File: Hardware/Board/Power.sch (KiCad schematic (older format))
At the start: 89 parts, among them Q1 Q_NMOS_DGS, Q2 Q_NMOS_DGS, Q3 Q_NMOS_DGS, Q4 Q_NMOS_DGS, U10 MAX17572, U11 MAX17572, U12 MAX17574, U16 STLD40D, U8 MAX17572, U9 MAX17572

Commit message: Trennung MCU und Rest, Footprints fast alles zugewiesen, GSM Modul integriert, viel Kleinkram
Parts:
- D1: footprint (none) -> Diode_SMD:D_SMB
- U16: footprint (none) -> Package_DFN_QFN:DFN-8-1EP_3x3mm_P0.65mm_EP1.55x2.4mm
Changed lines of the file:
@@
 F 0 "U16" H 3650 8125 50  0000 C CNN
 F 1 "STLD40D" H 3650 8034 50  0000 C CNN
-F 2 "" H 3650 8050 50  0001 C CNN
+F 2 "Package_DFN_QFN:DFN-8-1EP_3x3mm_P0.65mm_EP1.55x2.4mm" H 3650 8050 50  0001 C CNN
 F 3 "" H 3650 8050 50  0001 C CNN
 	1    3650 8050
@@
 F 0 "D1" H 4650 8015 50  0000 C CNN
 F 1 "DIODE" H 4650 7924 50  0000 C CNN
-F 2 "" H 4650 7750 50  0001 C CNN
+F 2 "Diode_SMD:D_SMB" H 4650 7750 50  0001 C CNN
 F 3 "~" H 4650 7750 50  0001 C CNN
 	1    4650 7750

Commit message: Footprints zuweisungen
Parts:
- removed Q1, Q2, Q3, Q4: Q_NMOS_DGS, symbol Device:Q_NMOS_DGS
- added Q1, Q2, Q3, Q4: 2N7002, Package_TO_SOT_SMD:SOT-23, symbol Transistor_FET:2N7002
- L1, L2, L3, L6: footprint (none) -> Inductor_SMD:L_Coilcraft_XxL4040
- L4: footprint (none) -> Inductor_SMD:L_Coilcraft_XxL4020
- L5: footprint (none) -> SamacSys_Parts:XAL8080
- L7: footprint (none) -> Inductor_SMD:L_Coilcraft_XxL4030
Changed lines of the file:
@@
 F 0 "L5" V 9840 1850 50  0000 C CNN
 F 1 "10uH" V 9749 1850 50  0000 C CNN
-F 2 "" H 9650 1850 50  0001 C CNN
+F 2 "SamacSys_Parts:XAL8080" H 9650 1850 50  0001 C CNN
 F 3 "~" H 9650 1850 50  0001 C CNN
 	1    9650 1850
@@
 	6700 1750 7050 1750
 $Comp
-L Device:Q_NMOS_DGS Q3
-U 1 1 5CA54BA8
-P 6950 2400
-AR Path="/5C8BBC9A/5CA54BA8" Ref="Q3"  Part="1"
-AR Path="/5E0C5EEA/5CA54BA8" Ref="Q?"  Part="1"
-F 0 "Q3" H 6750 2250 50  0000 L CNN
-F 1 "Q_NMOS_DGS" H 6550 2150 50  0000 L CNN
-F 2 "" H 7150 2500 50  0001 C CNN
-F 3 "~" H 6950 2400 50  0001 C CNN
-	1    6950 2400
-	1    0    0    -1
-$EndComp
-$Comp
 L power:GND #PWR0172
 U 1 1 5CA54C22
@@
 F 0 "L2" V 4840 3650 50  0000 C CNN
 F 1 "15uH" V 4749 3650 50  0000 C CNN
-F 2 "" H 4650 3650 50  0001 C CNN
+F 2 "Inductor_SMD:L_Coilcraft_XxL4040" H 4650 3650 50  0001 C CNN
 F 3 "~" H 4650 3650 50  0001 C CNN
 	1    4650 3650
@@
 F 0 "L1" V 4840 1600 50  0000 C CNN
 F 1 "15uH" V 4749 1600 50  0000 C CNN
-F 2 "" H 4650 1600 50  0001 C CNN
+F 2 "Inductor_SMD:L_Coilcraft_XxL4040" H 4650 1600 50  0001 C CNN
 F 3 "~" H 4650 1600 50  0001 C CNN
 	1    4650 1600
@@
 F 0 "L3" V 4840 5800 50  0000 C CNN
 F 1 "15uH" V 4749 5800 50  0000 C CNN
-F 2 "" H 4650 5800 50  0001 C CNN
+F 2 "Inductor_SMD:L_Coilcraft_XxL4040" H 4650 5800 50  0001 C CNN
 F 3 "~" H 4650 5800 50  0001 C CNN
 	1    4650 5800
@@
 	5100 6550 5100 6600
 $Comp
-L Device:Q_NMOS_DGS Q1
-U 1 1 5CAED088
-P 2200 4250
-AR Path="/5C8BBC9A/5CAED088" Ref="Q1"  Part="1"
-AR Path="/5E0C5EEA/5CAED088" Ref="Q?"  Part="1"
-F 0 "Q1" H 1700 4100 50  0000 L CNN
-F 1 "Q_NMOS_DGS" H 1650 4000 50  0000 L CNN
-F 2 "" H 2400 4350 50  0001 C CNN
-F 3 "~" H 2200 4250 50  0001 C CNN
-	1    2200 4250
-	1    0    0    -1
-$EndComp
-$Comp
 L power:GND #PWR0206
 U 1 1 5CAED08F
@@
 $EndComp
 $Comp
-L Device:Q_NMOS_DGS Q2
-U 1 1 5CB04AE3
-P 2200 6400
-AR Path="/5C8BBC9A/5CB04AE3" Ref="Q2"  Part="1"
-AR Path="/5E0C5EEA/5CB04AE3" Ref="Q?"  Part="1"
-F 0 "Q2" H 1700 6200 50  0000 L CNN
-F 1 "Q_NMOS_DGS" H 1650 6100 50  0000 L CNN
-F 2 "" H 2400 6500 50  0001 C CNN
-F 3 "~" H 2200 6400 50  0001 C CNN
-	1    2200 6400
-	1    0    0    -1
-$EndComp
-$Comp
 L power:GND #PWR0207
 U 1 1 5CB04AEA
@@
 F 0 "L4" V 8222 3450 50  0000 C CNN
 F 1 "L_Core_Ferrite" V 8313 3450 50  0000 C CNN
-F 2 "" H 8400 3450 50  0001 C CNN
+F 2 "Inductor_SMD:L_Coilcraft_XxL4020" H 8400 3450 50  0001 C CNN
 F 3 "~" H 8400 3450 50  0001 C CNN
 	1    8400 3450
@@
 F 0 "L6" V 9890 5000 50  0000 C CNN
 F 1 "15uH" V 9799 5000 50  0000 C CNN
-F 2 "" H 9700 5000 50  0001 C CNN
+F 2 "Inductor_SMD:L_Coilcraft_XxL4040" H 9700 5000 50  0001 C CNN
 F 3 "~" H 9700 5000 50  0001 C CNN
 	1    9700 5000
@@
 F 0 "L7" V 3840 7750 50  0000 C CNN
 F 1 "4uH7" V 3749 7750 50  0000 C CNN
-F 2 "" H 3650 7750 50  0001 C CNN
+F 2 "Inductor_SMD:L_Coilcraft_XxL4030" H 3650 7750 50  0001 C CNN
 F 3 "~" H 3650 7750 50  0001 C CNN
 	1    3650 7750
@@
 	7350 5350 7350 5400
 $Comp
-L Device:Q_NMOS_DGS Q4
-U 1 1 5D1E6DA4
+L Transistor_FET:2N7002 Q1
+U 1 1 5D17A6FC
+P 2200 4250
+F 0 "Q1" H 2405 4296 50  0000 L CNN
+F 1 "2N7002" H 2405 4205 50  0000 L CNN
+F 2 "Package_TO_SOT_SMD:SOT-23" H 2400 4175 50  0001 L CIN
+F 3 "https://www.fairchildsemi.com/datasheets/2N/2N7002.pdf" H 2200 4250 50  0001 L CNN
+	1    2200 4250
+	1    0    0    -1
+$EndComp
+$Comp
+L Transistor_FET:2N7002 Q2
+U 1 1 5D17AC62
+P 2200 6400
+F 0 "Q2" H 2405 6446 50  0000 L CNN
+F 1 "2N7002" H 2405 6355 50  0000 L CNN
+F 2 "Package_TO_SOT_SMD:SOT-23" H 2400 6325 50  0001 L CIN
+F 3 "https://www.fairchildsemi.com/datasheets/2N/2N7002.pdf" H 2200 6400 50  0001 L CNN
+	1    2200 6400
+	1    0    0    -1
+$EndComp
+$Comp
+L Transistor_FET:2N7002 Q4
+U 1 1 5D17AD96
 P 7250 5600
-AR Path="/5C8BBC9A/5D1E6DA4" Ref="Q4"  Part="1"
-AR Path="/5E0C5EEA/5D1E6DA4" Ref="Q?"  Part="1"
-F 0 "Q4" H 7050 5450 50  0000 L CNN
-F 1 "Q_NMOS_DGS" H 6700 5350 50  0000 L CNN
-F 2 "" H 7450 5700 50  0001 C CNN
-F 3 "~" H 7250 5600 50  0001 C CNN
+F 0 "Q4" H 7455 5646 50  0000 L CNN
+F 1 "2N7002" H 7455 5555 50  0000 L CNN
+F 2 "Package_TO_SOT_SMD:SOT-23" H 7450 5525 50  0001 L CIN
+F 3 "https://www.fairchildsemi.com/datasheets/2N/2N7002.pdf" H 7250 5600 50  0001 L CNN
 	1    7250 5600
 	1    0    0    -1
 $EndComp
+$Comp
+L Transistor_FET:2N7002 Q3
+U 1 1 5D17B2D6
+P 6950 2400
+F 0 "Q3" H 7155 2446 50  0000 L CNN
+F 1 "2N7002" H 7155 2355 50  0000 L CNN
+F 2 "Package_TO_SOT_SMD:SOT-23" H 7150 2325 50  0001 L CIN
+F 3 "https://www.fairchildsemi.com/datasheets/2N/2N7002.pdf" H 6950 2400 50  0001 L CNN
+	1    6950 2400
+	1    0    0    -1
+$EndComp

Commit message: Komplete enummerierung Geändert, Schaltplan zusammengefasst, Layout nochmals reset. BOM zu 75% fertig gestellt
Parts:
- added D101, D102: B345BE-13, Diode_SMD:D_SMB, symbol pspice:DIODE
- C100: renamed from C26; footprint Capacitor_SMD:C_0603_1608Metric -> Capacitor_SMD:C_1210_3225Metric
- C105: renamed from C27; footprint Capacitor_SMD:C_0603_1608Metric -> Capacitor_SMD:C_1210_3225Metric
- C111: renamed from C28; footprint Capacitor_SMD:C_0603_1608Metric -> Capacitor_SMD:C_1210_3225Metric
- C117: renamed from C67; footprint Capacitor_SMD:C_0603_1608Metric -> Capacitor_SMD:C_1210_3225Metric
- C119: renamed from C69; footprint Capacitor_SMD:C_0603_1608Metric -> Capacitor_SMD:C_1210_3225Metric
- C120: renamed from C40; footprint Capacitor_SMD:C_0603_1608Metric -> Capacitor_SMD:C_1210_3225Metric
- C121: renamed from C41; footprint Capacitor_SMD:C_0603_1608Metric -> Capacitor_SMD:C_1210_3225Metric
- C132: renamed from C42; footprint Capacitor_SMD:C_0603_1608Metric -> Capacitor_SMD:C_1210_3225Metric
- D100: renamed from D1; value DIODE -> B345BE-13
- renumbered C33 to C101, C37 to C102, C29 to C104, C32 to C106, C34 to C107, C38 to C108, C36 to C109, C30 to C110, C35 to C112, C39 to C113, C31 to C114, C65 to C115, C66 to C116, C68 to C118, C44 to C122, C48 to C123, C56 to C124, C54 to C125, C57 to C126, C51 to C127, C43 to C128, C45 to C129, C49 to C130, C53 to C131, C46 to C133, C47 to C134, C50 to C135, C55 to C136, C52 to C137, FB16 to FB100, FB17 to FB101, L1 to L100, L2 to L101, L3 to L102, L7 to L103, L5 to L104, L4 to L105, L6 to L106, Q1 to Q100, Q2 to Q102, Q3 to Q103, Q4 to Q104, R14 to R100, R15 to R101, R18 to R102, R22 to R103, R23 to R104, R12 to R105, R16 to R106, R19 to R107, R21 to R108, R24 to R109, R25 to R110, R13 to R111, R17 to R112, R20 to R113, R26 to R114, R27 to R115, R50 to R116, R51 to R117, R52 to R118, R28 to R119, R30 to R120, R32 to R121, R35 to R122, R38 to R123, R39 to R124, R29 to R125, R31 to R126, R33 to R127, R36 to R128, R37 to R129, R34 to R130, U8 to U100, U9 to U101, U10 to U102, U16 to U103, U12 to U104, U11 to U105
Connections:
- net DC_Input: now also D101.2 (A), D102.2 (A)
- net GND: now also D101.1 (K), D102.1 (K)
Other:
- moved on the sheet: C128, C129

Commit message: Bauteil Gruppierungen im Layout
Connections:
- net +BATT: now also L105.1; no longer F1.1
- net DC_Input: now also F1.2; no longer D101.2 (A), D102.2 (A), L105.2
- new net: D101.2 (A), D102.2 (A), F1.1, L105.2
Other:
- moved on the sheet: D101, D102, F1, L105
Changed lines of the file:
@@
 L Device:L_Core_Ferrite L105
 U 1 1 5CB6DCC1
-P 8400 3450
+P 8700 3450
 AR Path="/5C8BBC9A/5CB6DCC1" Ref="L105"  Part="1"
 AR Path="/5E0C5EEA/5CB6DCC1" Ref="L?"  Part="1"
-F 0 "L105" V 8200 3550 50  0000 C CNN
-F 1 "L_Core_Ferrite" V 8300 3550 50  0000 C CNN
-F 2 "Inductor_SMD:L_Coilcraft_XxL4020" H 8400 3450 50  0001 C CNN
-F 3 "~" H 8400 3450 50  0001 C CNN
-	1    8400 3450
+F 0 "L105" V 8500 3550 50  0000 C CNN
+F 1 "L_Core_Ferrite" V 8600 3550 50  0000 C CNN
+F 2 "Inductor_SMD:L_Coilcraft_XxL4020" H 8700 3450 50  0001 C CNN
+F 3 "~" H 8700 3450 50  0001 C CNN
+	1    8700 3450
 	0    1    1    0
 $EndComp
@@
 L Device:Fuse F1
 U 1 1 5CB6DEB6
-P 8950 3450
+P 7500 3450
 AR Path="/5C8BBC9A/5CB6DEB6" Ref="F1"  Part="1"
 AR Path="/5E0C5EEA/5CB6DEB6" Ref="F?"  Part="1"
-F 0 "F1" V 8753 3450 50  0000 C CNN
-F 1 "KFZ 5A" V 8844 3450 50  0000 C CNN
-F 2 "Fuse:Fuseholder_Blade_ATO_Littelfuse_Pudenz_2_Pin" V 8880 3450 50  0001 C CNN
-F 3 "~" H 8950 3450 50  0001 C CNN
-	1    8950 3450
+F 0 "F1" V 7303 3450 50  0000 C CNN
+F 1 "KFZ 5A" V 7394 3450 50  0000 C CNN
+F 2 "Fuse:Fuseholder_Blade_ATO_Littelfuse_Pudenz_2_Pin" V 7430 3450 50  0001 C CNN
+F 3 "~" H 7500 3450 50  0001 C CNN
+	1    7500 3450
 	0    1    1    0
 $EndComp
@@
 $EndComp
 Wire Wire Line
-	9100 3450 9400 3450
-Wire Wire Line
 	9650 3450 9400 3450
 Connection ~ 9400 3450
@@
 Connection ~ 9650 3450
 Wire Wire Line
-	8800 3450 8550 3450
-Wire Wire Line
 	6800 3450 7100 3450
-Connection ~ 7100 3450
 Text GLabel 6700 3450 0    50   Input ~ 0
 DC_Input
@@
 L pspice:DIODE D101
 U 1 1 5D54A227
-P 7650 3650
+P 7950 3650
 AR Path="/5C8BBC9A/5D54A227" Ref="D101"  Part="1"
 AR Path="/5E0C5EEA/5D54A227" Ref="D?"  Part="1"
-F 0 "D101" V 8150 4000 50  0000 C CNN
-F 1 "B345BE-13" V 8050 3900 50  0000 C CNN
-F 2 "Diode_SMD:D_SMB" H 7650 3650 50  0001 C CNN
-F 3 "~" H 7650 3650 50  0001 C CNN
-	1    7650 3650
-	0    -1   -1   0
-$EndComp
-$Comp
-L pspice:DIODE D102
-U 1 1 5D584B01
-P 7950 3650
-AR Path="/5C8BBC9A/5D584B01" Ref="D102"  Part="1"
-AR Path="/5E0C5EEA/5D584B01" Ref="D?"  Part="1"
-F 0 "D102" V 8450 3800 50  0000 C CNN
-F 1 "B345BE-13" V 8350 3700 50  0000 C CNN
+F 0 "D101" V 8450 4000 50  0000 C CNN
+F 1 "B345BE-13" V 8350 3900 50  0000 C CNN
 F 2 "Diode_SMD:D_SMB" H 7950 3650 50  0001 C CNN
 F 3 "~" H 7950 3650 50  0001 C CNN
@@
 $EndComp
 $Comp
+L pspice:DIODE D102
+U 1 1 5D584B01
+P 8250 3650
+AR Path="/5C8BBC9A/5D584B01" Ref="D102"  Part="1"
+AR Path="/5E0C5EEA/5D584B01" Ref="D?"  Part="1"
+F 0 "D102" V 8750 3800 50  0000 C CNN
+F 1 "B345BE-13" V 8650 3700 50  0000 C CNN
+F 2 "Diode_SMD:D_SMB" H 8250 3650 50  0001 C CNN
+F 3 "~" H 8250 3650 50  0001 C CNN
+	1    8250 3650
+	0    -1   -1   0
+$EndComp
+$Comp
 L power:GND #PWR0380
 U 1 1 5D5917AD
-P 7650 3850
+P 7950 3850
 AR Path="/5C8BBC9A/5D5917AD" Ref="#PWR0380"  Part="1"
 AR Path="/5E0C5EEA/5D5917AD" Ref="#PWR?"  Part="1"
-F 0 "#PWR0380" H 7650 3600 50  0001 C CNN
-F 1 "GND" H 7655 3677 50  0000 C CNN
-F 2 "" H 7650 3850 50  0001 C CNN
-F 3 "" H 7650 3850 50  0001 C CNN
-	1    7650 3850
-	1    0    0    -1
-$EndComp
-$Comp
-L power:GND #PWR0381
-U 1 1 5D59D0F4
-P 7950 3850
-AR Path="/5C8BBC9A/5D59D0F4" Ref="#PWR0381"  Part="1"
-AR Path="/5E0C5EEA/5D59D0F4" Ref="#PWR?"  Part="1"
-F 0 "#PWR0381" H 7950 3600 50  0001 C CNN
+F 0 "#PWR0380" H 7950 3600 50  0001 C CNN
 F 1 "GND" H 7955 3677 50  0000 C CNN
 F 2 "" H 7950 3850 50  0001 C CNN
@@
 	1    0    0    -1
 $EndComp
+$Comp
+L power:GND #PWR0381
+U 1 1 5D59D0F4
+P 8250 3850
+AR Path="/5C8BBC9A/5D59D0F4" Ref="#PWR0381"  Part="1"
+AR Path="/5E0C5EEA/5D59D0F4" Ref="#PWR?"  Part="1"
+F 0 "#PWR0381" H 8250 3600 50  0001 C CNN
+F 1 "GND" H 8255 3677 50  0000 C CNN
+F 2 "" H 8250 3850 50  0001 C CNN
+F 3 "" H 8250 3850 50  0001 C CNN
+	1    8250 3850
+	1    0    0    -1
+$EndComp
+Wire Wire Line
+	8550 3450 8250 3450
 Wire Wire Line
 	8250 3450 7950 3450
-Wire Wire Line
-	7950 3450 7650 3450
+Connection ~ 8250 3450
+Wire Wire Line
+	8850 3450 9400 3450
+Wire Wire Line
+	7650 3450 7950 3450
 Connection ~ 7950 3450
 Wire Wire Line
-	7100 3450 7650 3450
-Connection ~ 7650 3450
+	7350 3450 7100 3450
+Connection ~ 7100 3450
 $EndSCHEMATC

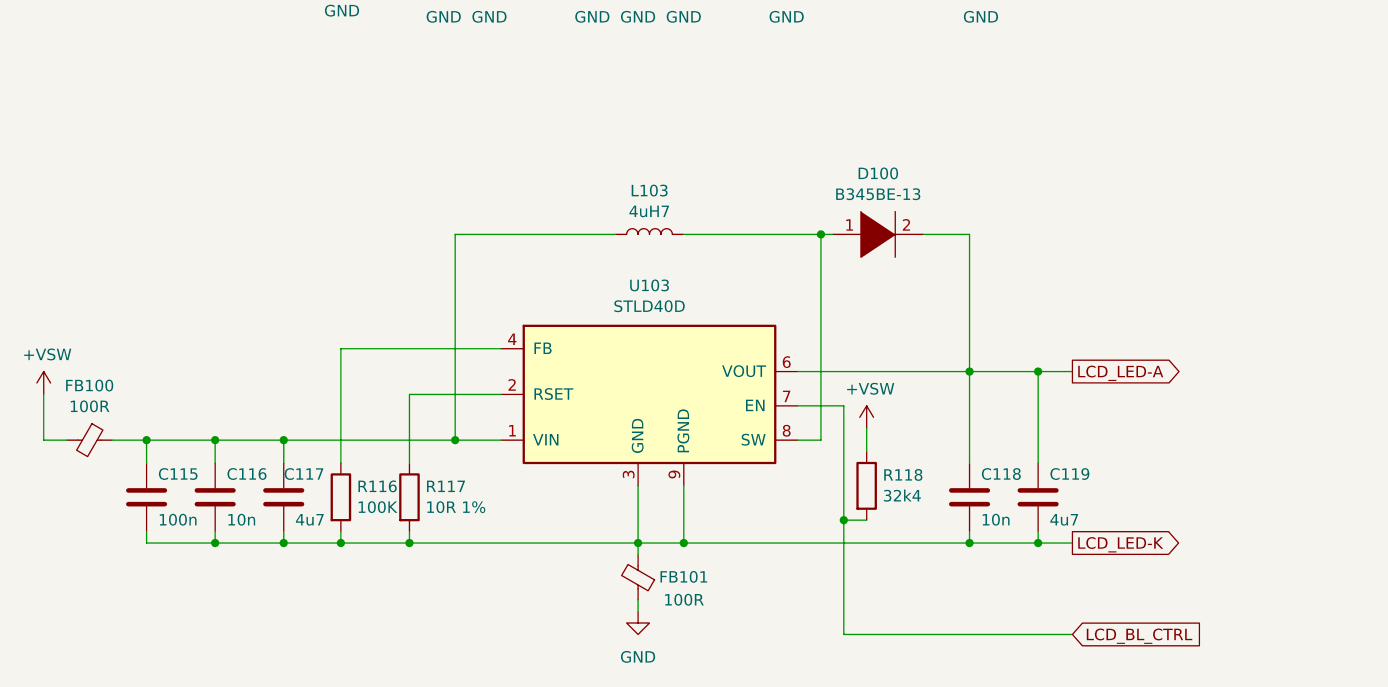
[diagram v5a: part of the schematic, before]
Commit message: Änderung des Konzeptes auf 2 Boards, eines TFT Touch mit STM32L4R9, das rein die Bedienung macht. Control Board mit STM32L476, mit noch mehr Schnittstellen. Bus zwischen Display, Board, Raspberry/ESP ist RS485, Bus als RJ45 mit Wakeup und Stromversorgung
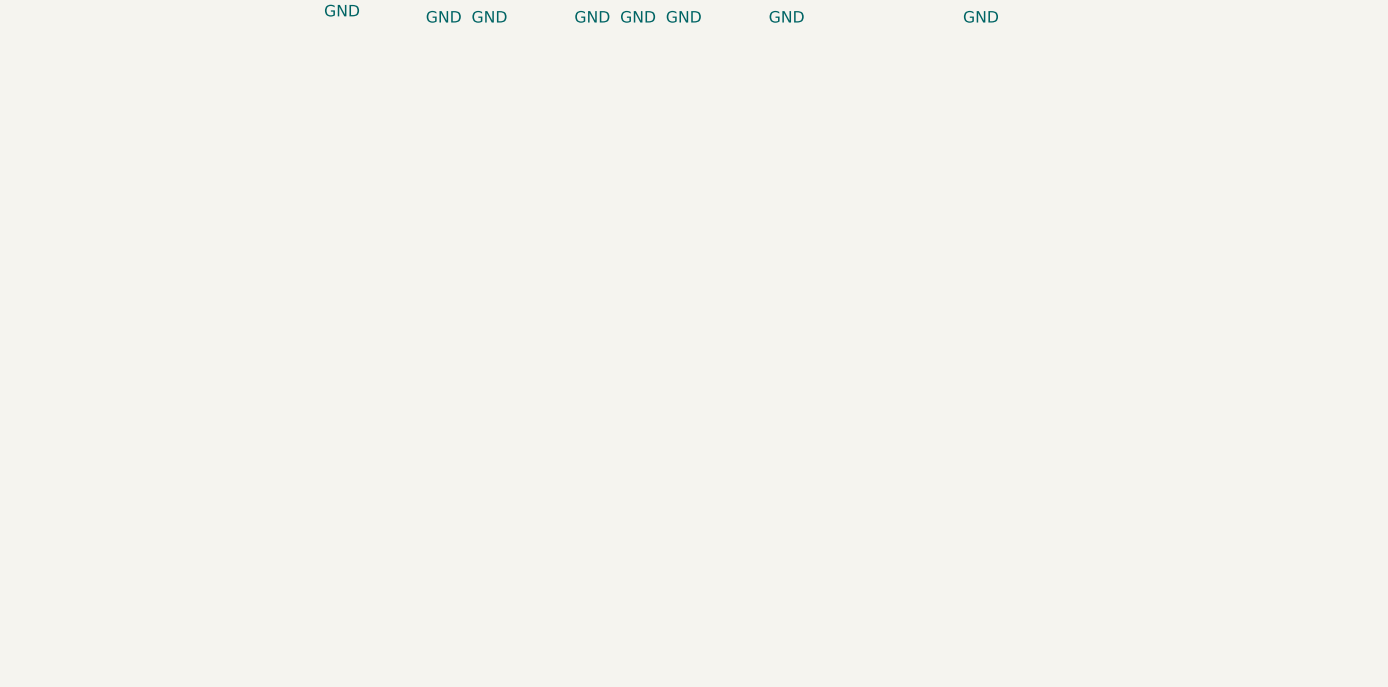
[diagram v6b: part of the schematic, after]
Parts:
- removed C115: 100n, Capacitor_SMD:C_0603_1608Metric, symbol Device:C
- removed C116, C118: 10n, Capacitor_SMD:C_0603_1608Metric, symbol Device:C
- removed C117, C119: 4u7, Capacitor_SMD:C_1210_3225Metric, symbol Device:C
- removed D100: B345BE-13, Diode_SMD:D_SMB, symbol pspice:DIODE
- removed FB100, FB101: 100R, Inductor_SMD:L_0603_1608Metric, symbol Device:Ferrite_Bead_Small
- removed L103: 4uH7, Inductor_SMD:L_Coilcraft_XxL4030, symbol Device:L
- removed R116: 100K, Resistor_SMD:R_0603_1608Metric, symbol Device:R
- removed R117: 10R 1%, Resistor_SMD:R_0603_1608Metric, symbol Device:R
- removed R118: 32k4, Resistor_SMD:R_0603_1608Metric, symbol Device:R
- removed U103: STLD40D, Package_DFN_QFN:DFN-8-1EP_3x3mm_P0.65mm_EP1.55x2.4mm, symbol Womo-rescue:STLD40D-DC_DC_Wandler
